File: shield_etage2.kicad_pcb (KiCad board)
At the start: 2 copper layers, 70.6 x 83.1 mm, 60 parts, among them J1 Conn_01x02, J10 ToF, J11 Moteur, J12 Moteur, J13 butee, J14 Moteur, J15 butee, J16 butee, J17 Conn_01x03-Connector_Generic-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, J19 output_CAN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

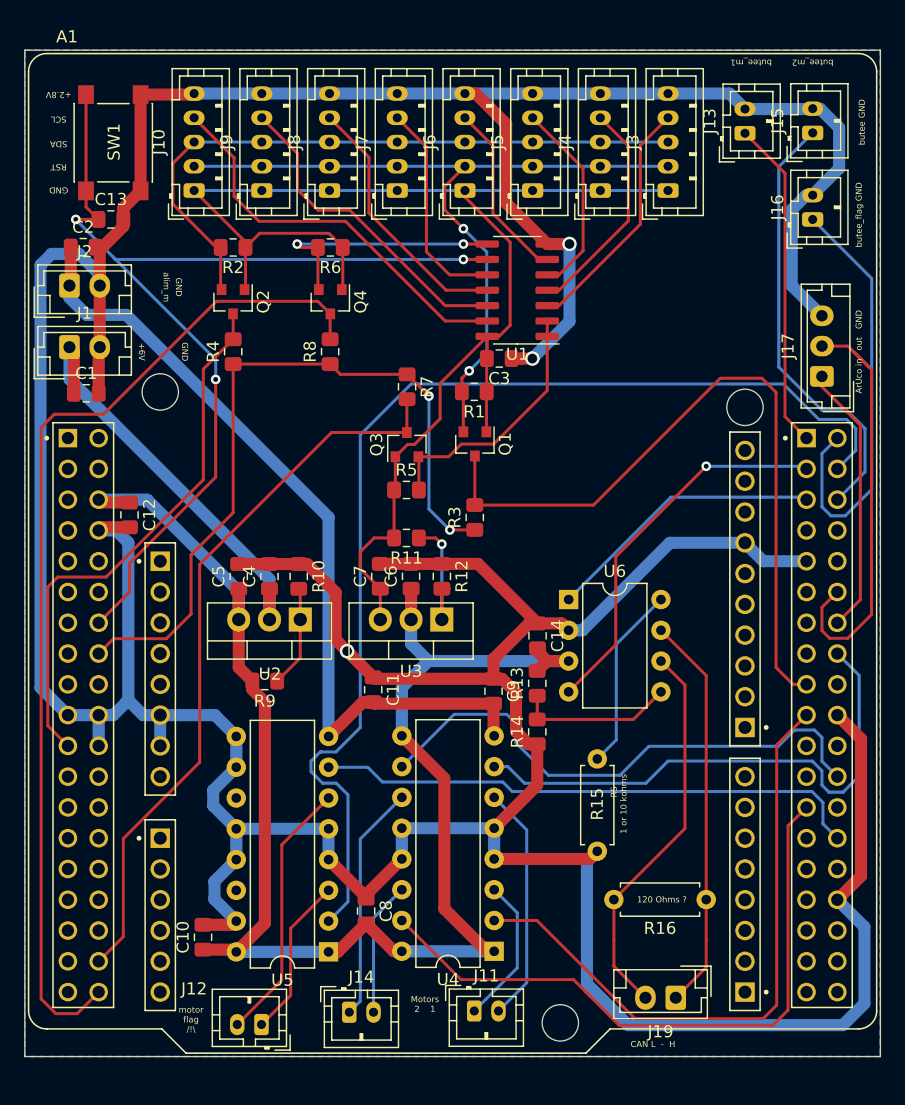
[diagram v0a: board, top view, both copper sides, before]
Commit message: correction mm -> inch, empreinte du bouton
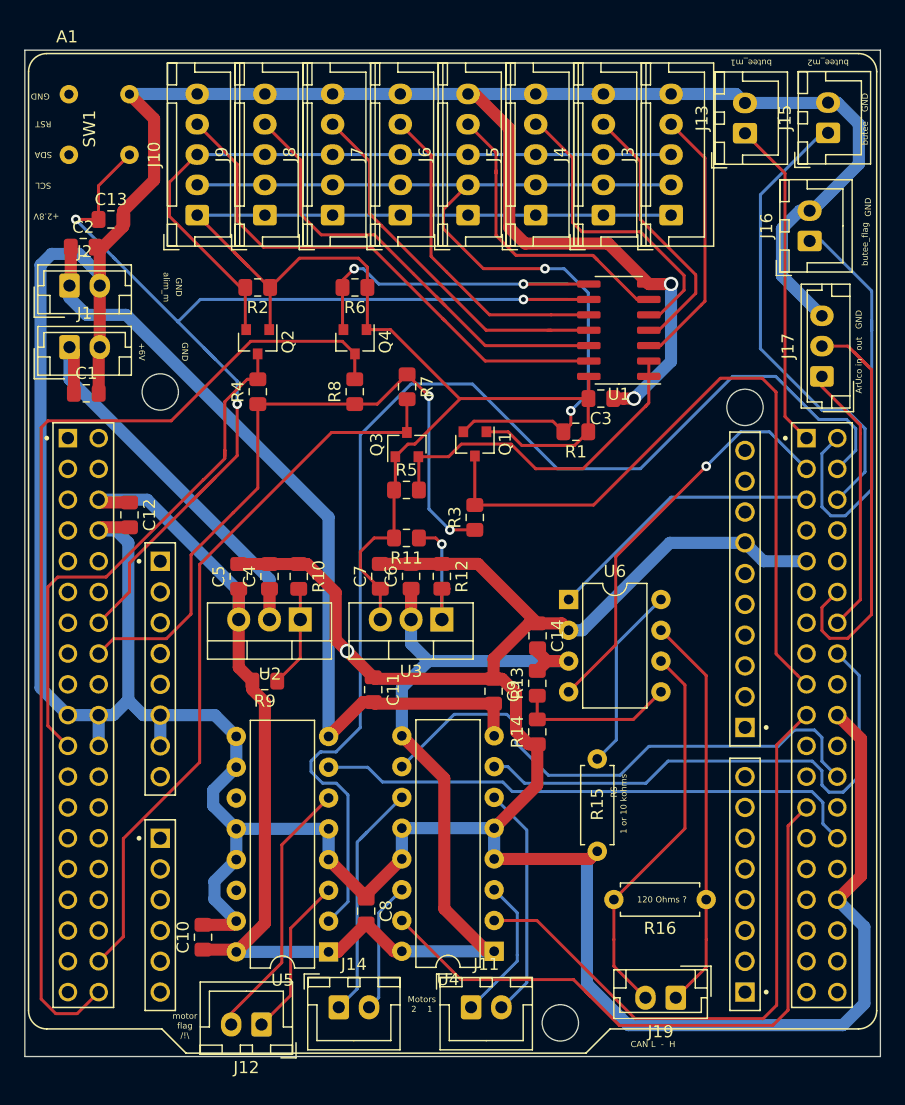
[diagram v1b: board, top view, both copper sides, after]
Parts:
- J10, J3, J4, J5, J6, J7, J8, J9: footprint Connector_JST:JST_PH_B5B-PH-K_1x05_P2.00mm_Vertical -> Connector_JST:JST_XH_B5B-XH-A_1x05_P2.50mm_Vertical
- J11, J12, J13, J14, J15, J16: footprint Connector_JST:JST_PH_B2B-PH-K_1x02_P2.00mm_Vertical -> Connector_JST:JST_XH_B2B-XH-A_1x02_P2.50mm_Vertical
- SW1: footprint Button_Switch_SMD:SW_Push_1P1T_NO_6x6mm_H9.5mm -> button:5x5
- moved C3 9.01 mm to (203.5, 101.7)
- moved R1 9.01 mm to (201.4, 104.4)
- moved U1 9.01 mm to (205.0, 96.0)
- moved R2 3.88 mm to (175.2, 92.5)
- moved R6 3.88 mm to (183.2, 92.5)
- moved Q2 3.88 mm to (175.2, 97.0)
- moved Q4 3.88 mm to (183.2, 97.0)
- moved R4 3.88 mm to (175.2, 101.1)
- moved R8 3.88 mm to (183.2, 101.1)
- moved J10 2.05 mm to (170.2, 86.5)
- moved J6 2.05 mm to (192.5, 86.5)
- moved J3 2.05 mm to (209.3, 86.5)
- moved J4 2.05 mm to (203.7, 86.5)
- moved J5 2.05 mm to (198.1, 86.5)
- moved J7 2.05 mm to (186.9, 86.5)
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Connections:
- A1 pad CN10_11: (no net) -> Net-(A1-PadCN10_11)
- A1 pad CN10_13: (no net) -> Net-(A1-PadCN10_13)
- A1 pad CN10_15: (no net) -> Net-(A1-PadCN10_15)
- A1 pad CN10_21: (no net) -> Net-(A1-PadCN10_21)
- A1 pad CN10_22: (no net) -> Net-(A1-PadCN10_22)
- A1 pad CN10_23: (no net) -> Net-(A1-PadCN10_23)
- A1 pad CN10_26: (no net) -> Net-(A1-PadCN10_26)
- A1 pad CN10_27: (no net) -> Net-(A1-PadCN10_27)
- A1 pad CN10_29: (no net) -> Net-(A1-PadCN10_29)
- A1 pad CN10_30: (no net) -> Net-(A1-PadCN10_30)
- A1 pad CN10_31: (no net) -> Net-(A1-PadCN10_31)
- A1 pad CN10_33: (no net) -> Net-(A1-PadCN10_33)
- A1 pad CN10_34: (no net) -> Net-(A1-PadCN10_34)
- A1 pad CN10_35: (no net) -> Net-(A1-PadCN10_35)
- A1 pad CN10_37: (no net) -> Net-(A1-PadCN10_37)
- A1 pad CN10_7: (no net) -> Net-(A1-PadCN10_7)
- A1 pad CN10_8: (no net) -> Net-(A1-PadCN10_8)
- A1 pad CN5_1: (no net) -> Net-(A1-PadCN5_1)
- A1 pad CN5_10: (no net) -> Net-(A1-PadCN5_10)
- A1 pad CN5_2: (no net) -> Net-(A1-PadCN5_2)
- A1 pad CN5_3: (no net) -> Net-(A1-PadCN5_3)
- A1 pad CN5_4: (no net) -> Net-(A1-PadCN5_4)
- A1 pad CN5_5: (no net) -> Net-(A1-PadCN5_5)
- A1 pad CN5_6: (no net) -> Net-(A1-PadCN5_6)
- A1 pad CN5_8: (no net) -> Net-(A1-PadCN5_8)
- A1 pad CN5_9: (no net) -> Net-(A1-PadCN5_9)
- A1 pad CN6_2: (no net) -> Net-(A1-PadCN6_2)
- A1 pad CN6_3: (no net) -> Net-(A1-PadCN6_3)
- A1 pad CN6_4: (no net) -> Net-(A1-PadCN6_4)
- A1 pad CN6_5: (no net) -> Net-(A1-PadCN6_5)
- A1 pad CN6_8: (no net) -> Net-(A1-PadCN6_8)
- A1 pad CN7_1: (no net) -> Net-(A1-PadCN7_1)
- A1 pad CN7_12: (no net) -> Net-(A1-PadCN7_12)
- A1 pad CN7_13: (no net) -> Net-(A1-PadCN7_13)
- A1 pad CN7_15: (no net) -> Net-(A1-PadCN7_15)
- A1 pad CN7_17: (no net) -> Net-(A1-PadCN7_17)
- A1 pad CN7_18: (no net) -> Net-(A1-PadCN7_18)
- A1 pad CN7_2: (no net) -> Net-(A1-PadCN7_2)
- A1 pad CN7_23: (no net) -> Net-(A1-PadCN7_23)
- A1 pad CN7_24: (no net) -> Net-(A1-PadCN7_24)
- A1 pad CN7_25: (no net) -> Net-(A1-PadCN7_25)
- A1 pad CN7_27: (no net) -> Net-(A1-PadCN7_27)
- A1 pad CN7_28: (no net) -> Net-(A1-PadCN7_28)
- A1 pad CN7_29: (no net) -> Net-(A1-PadCN7_29)
- A1 pad CN7_3: (no net) -> Net-(A1-PadCN7_3)
- A1 pad CN7_30: (no net) -> Net-(A1-PadCN7_30)
- A1 pad CN7_31: (no net) -> Net-(A1-PadCN7_31)
- A1 pad CN7_32: (no net) -> Net-(A1-PadCN7_32)
- A1 pad CN7_33: (no net) -> Net-(A1-PadCN7_33)
- A1 pad CN7_34: (no net) -> Net-(A1-PadCN7_34)
- A1 pad CN7_35: (no net) -> Net-(A1-PadCN7_35)
- A1 pad CN7_37: (no net) -> Net-(A1-PadCN7_37)
- A1 pad CN7_4: (no net) -> Net-(A1-PadCN7_4)
- A1 pad CN7_5: (no net) -> Net-(A1-PadCN7_5)
- A1 pad CN7_7: (no net) -> Net-(A1-PadCN7_7)
- A1 pad CN8_1: (no net) -> Net-(A1-PadCN8_1)
- A1 pad CN8_2: (no net) -> Net-(A1-PadCN8_2)
- A1 pad CN8_3: (no net) -> Net-(A1-PadCN8_3)
- A1 pad CN8_4: (no net) -> Net-(A1-PadCN8_4)
- A1 pad CN8_5: (no net) -> Net-(A1-PadCN8_5)
- A1 pad CN8_6: (no net) -> Net-(A1-PadCN8_6)
- A1 pad CN9_1: (no net) -> Net-(A1-PadCN9_1)
- A1 pad CN9_2: (no net) -> Net-(A1-PadCN9_2)
- A1 pad CN9_3: (no net) -> Net-(A1-PadCN9_3)
- A1 pad CN9_4: (no net) -> Net-(A1-PadCN9_4)
- A1 pad CN9_5: (no net) -> Net-(A1-PadCN9_5)
- A1 pad CN9_6: (no net) -> Net-(A1-PadCN9_6)
- A1 pad CN9_7: (no net) -> Net-(A1-PadCN9_7)
- A1 pad CN9_8: (no net) -> Net-(A1-PadCN9_8)
- U5 pad 11: (no net) -> Net-(U5-Pad11)
- U5 pad 14: (no net) -> Net-(U5-Pad14)
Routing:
- net GND: track 434.2 -> 450.7 mm
- net /LevelShifter_ToF_I2C/I2C_SCL_ToF: track 64.1 -> 79.0 mm
- net +2V8: track 114.1 -> 126.9 mm
- net /ShiftRegister/Reset_ToF_6: track 26.8 -> 38.2 mm
- net /ShiftRegister/Reset_ToF_3: track 14.9 -> 26.3 mm
- net /ShiftRegister/Reset_ToF_7: track 33.0 -> 43.4 mm
- net /ShiftRegister/Reset_ToF_5: track 21.6 -> 31.5 mm
- net /ShiftRegister/Reset_ToF_4: track 17.9 -> 27.0 mm
- net /ShiftRegister/Reset_ToF_2: track 16.5 -> 25.5 mm
- net /F4/NRST: track 85.9 -> 94.5 mm
- net /LevelShifter_ShiftRegister/ShiftRegister_CP: track 21.0 -> 29.1 mm
- net /LevelShifter_ShiftRegister/ShiftRegister_DSAB: track 21.4 -> 28.9 mm
- net /Driver_moteurs/pwm_drapeau: track 93.3 -> 99.6 mm
- net /LevelShifter_ToF_I2C/I2C_SDA_ToF: track 53.9 -> 57.7 mm
- net +3V3: track 62.1 -> 58.3 mm
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- removed copper zone on B.Cu, net GND
- removed copper zone on F.Cu, net GND
